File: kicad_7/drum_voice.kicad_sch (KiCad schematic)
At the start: 12 parts, among them J11 AudioJack2_SwitchT, SW5 SW_SPDT_MSM, SW6 SW_Rotary3x4, SW7 SW_Rotary3x4, U53 TL072

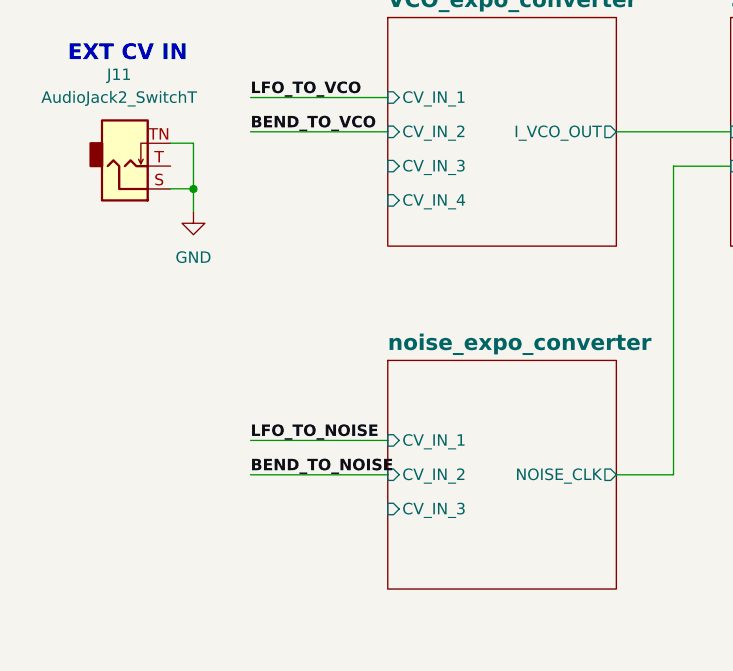
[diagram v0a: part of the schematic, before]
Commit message: Fix external CV input circuit
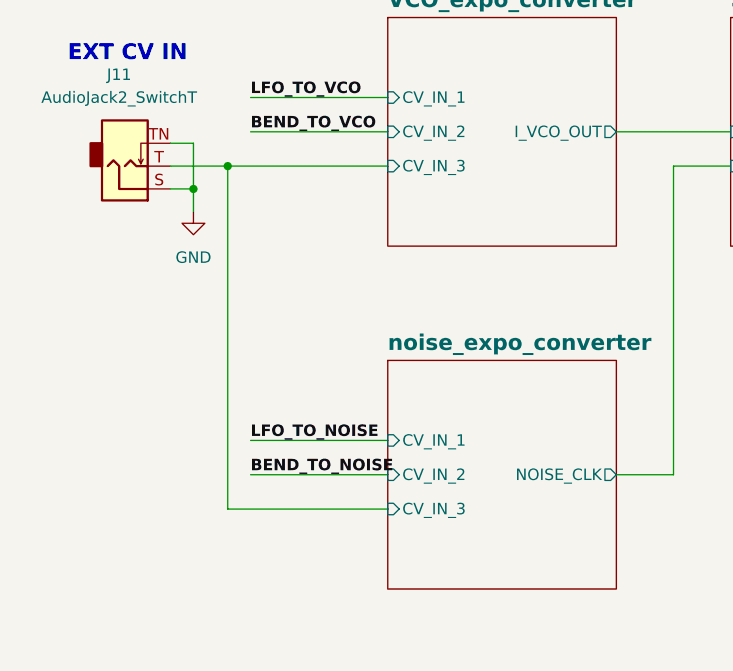
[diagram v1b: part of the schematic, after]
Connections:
- net VCO_expo_converter/CV_IN_3: now also J11.T
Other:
- sheet VCO_expo_converter ports: added none; removed CV_IN_4
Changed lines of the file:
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@@
-(kicad_sch (version 20221206) (generator eeschema)
+(kicad_sch (version 20230121) (generator eeschema)
   (paper "A4")
   (title_block
@@
   )
   (junction (at 38.1 173.99) (diameter 0) (color 0 0 0 0)
+  )
+  (junction (at 33.02 54.61) (diameter 0) (color 0 0 0 0)
   )
   (junction (at 49.53 161.29) (diameter 0) (color 0 0 0 0)
@@
     (stroke (width 0) (type default))
   )
+  (wire (pts (xy 33.02 54.61) (xy 50.8 54.61))
+    (stroke (width 0) (type default))
+  )
   (wire (pts (xy 38.1 184.15) (xy 38.1 186.69))
     (stroke (width 0) (type default))
@@
     (stroke (width 0) (type default))
   )
+  (wire (pts (xy 26.67 54.61) (xy 33.02 54.61))
+    (stroke (width 0) (type default))
+  )
   (wire (pts (xy 135.89 173.99) (xy 151.13 173.99))
     (stroke (width 0) (type default))
@@
     (stroke (width 0) (type default))
   )
+  (wire (pts (xy 33.02 54.61) (xy 33.02 92.71))
+    (stroke (width 0) (type default))
+  )
   (wire (pts (xy 106.68 176.53) (xy 110.49 176.53))
+    (stroke (width 0) (type default))
+  )
+  (wire (pts (xy 50.8 92.71) (xy 33.02 92.71))
     (stroke (width 0) (type default))
   )
@@
       (effects (font (size 1.27 1.27)) (justify left top) hide)
     )
-    (pin "CV_IN_4" input (at 50.8 58.42 180)
-      (effects (font (size 1.27 1.27)) (justify left))
-    )
     (pin "CV_IN_1" input (at 50.8 46.99 180)
